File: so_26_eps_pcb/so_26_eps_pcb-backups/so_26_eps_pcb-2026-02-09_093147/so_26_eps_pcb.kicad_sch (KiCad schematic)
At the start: 84 parts, among them J1 Conn_02x12_Odd_Even, J2 Conn_01x02, SW1 SW_SPDT

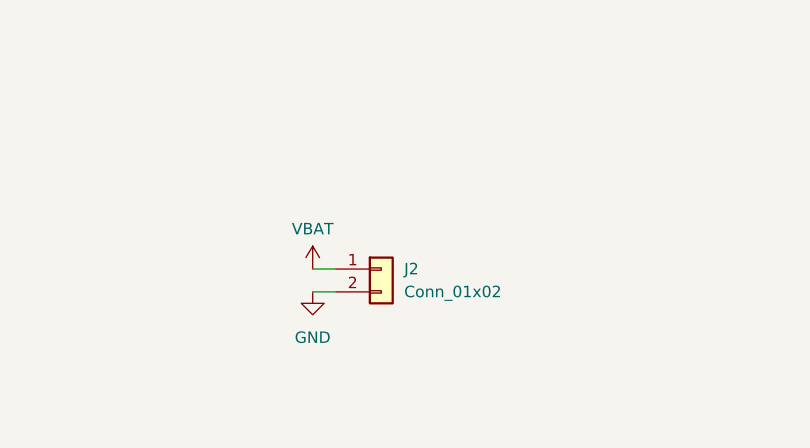
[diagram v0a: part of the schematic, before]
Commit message: Updated some footprints
Deleted some old components and changed the size on the testpoints from 2mm in diameters to 1.5mm in diameters
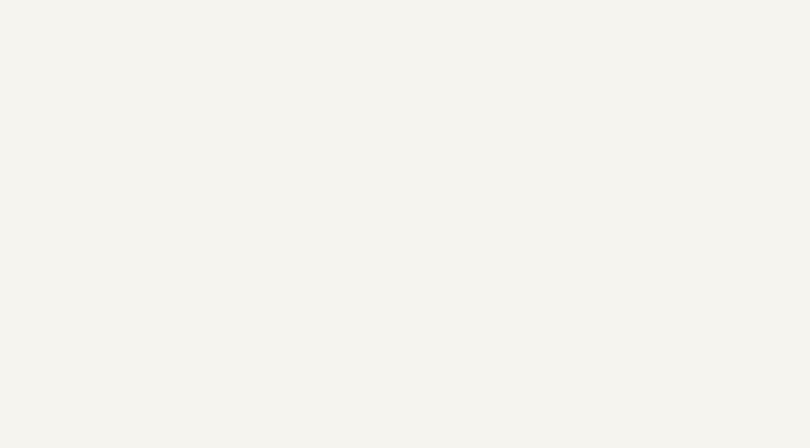
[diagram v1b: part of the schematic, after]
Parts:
- removed J2: Conn_01x02, Myfootprints:01x02_header, symbol Connector_Generic:Conn_01x02
- TP1, TP10, TP11, TP12, TP13, TP14, TP15, TP16, TP17, TP18, TP19, TP2, TP20, TP21, TP22, TP23, TP24, TP25, TP26, TP27, TP28, TP29, TP3, TP30, TP31, TP32, TP33, TP34, TP35, TP36, TP37, TP4, TP5, TP6, TP7, TP8, TP9: footprint TestPoint:TestPoint_Pad_D1.5mm -> TestPoint:TestPoint_Pad_D2.0mm
